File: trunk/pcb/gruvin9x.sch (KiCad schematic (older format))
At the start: 162 parts, among them K1 CONN_3, K2 CONN_3, P1 CONN_5X2, P10 CONN_1, P11 CONN_1, P12 CONN_1, P13 CONN_8, P14 CONN_2, P15 CONN_1, P16 CONN_1, P17 CONN_1, P2 CONN_5, P3 CONN_6, P4 CONN_9, P5 CONN_9, P6 CONN_6, P7 CONN_12, P8 CONN_30, P9 CONN_1, Q1 BC847C, Q2 BC847C, Q3 BC857C, SW1 SW_PUSH, SW2 SW_PUSH, SW3 SW_PUSH, SW4 SW_PUSH, SW5 SW_PUSH, SW6 SW_PUSH, U1 78L05, U2 4066, U3 LN-6206-30, X1 16MHz 18pf

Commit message: Issue 17 fixed
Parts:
- gave numbers to parts that had none: 4
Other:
- note added: "Trim Switches"
- note removed: "Trim Switches (existing wires)"

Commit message: PCB V3 re-routed to corrected V3 schematic (trims + PPM-in inverting buffer). Corrections made to LCD decoupling capacitor values (1uF) on other schematics.
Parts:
- removed C53, C54, C55, C56: 0.1, symbol C
- removed Q4: BC549, SOT23EBD, symbol NPN
- added Q4: BC847C, SOT23-BCE, symbol BC847C
- C46, C47, C48, C49, C50: value 0.1 -> 1u
- R79: value 330 -> 200
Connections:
- wire segments 519 -> 510

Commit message: Code, Schematic and PCB updated to new Timer0 WGM speaker tone output on PB7. (Backlight control moved to PC0. Old timer0 stuff moved to timer2)
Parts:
- removed P15: CONN_1, symbol CONN_1
- added P18: CONN_2, CONN_2MM_2x1, symbol CONN_2
- added R82: 1K0, symbol R
- added R83, R84: 200, symbol R
- P14: footprint (none) -> CONN_2MM_2x1
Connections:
- net labels added: Buzzer, Volume
- net labels removed: Spare2
- wire segments 510 -> 511
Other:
- moved on the sheet: P10

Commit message: Schematic v3.2 updated to include LCD back-light driver mounting posts. PCB v3.2 routed to match.
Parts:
- removed P12: CONN_1, symbol CONN_1
- added K3: CONN_3, symbol CONN_3
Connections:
- wire segments 511 -> 517

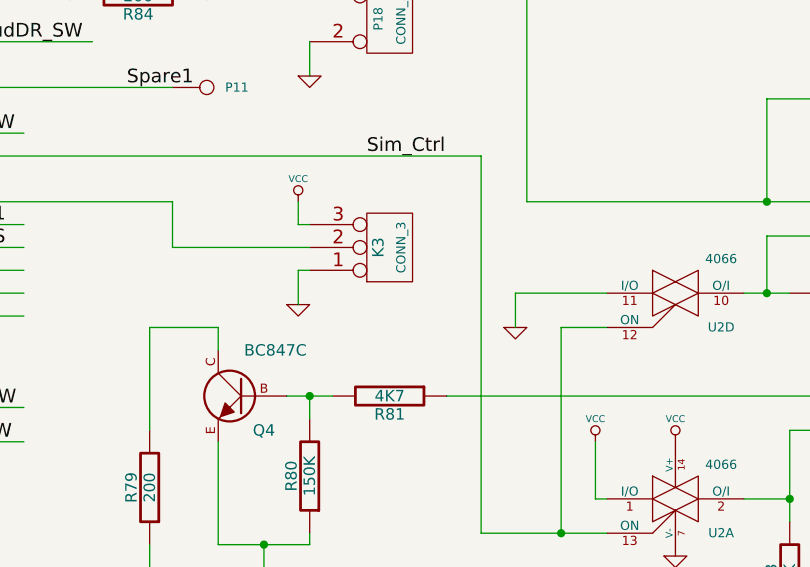
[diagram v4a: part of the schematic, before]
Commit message: Minor V3 schematic edit
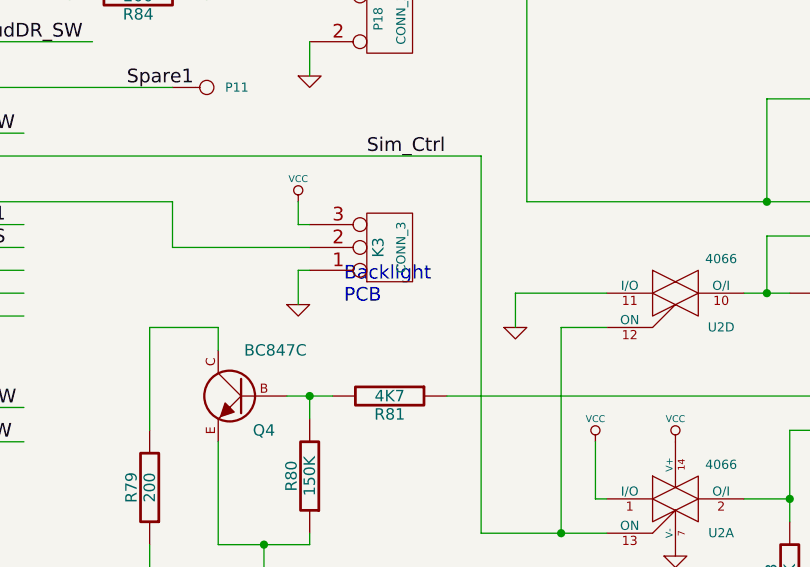
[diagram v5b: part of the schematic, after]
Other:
- note added: "Backlight\nPCB"
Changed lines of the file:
@@
-EESchema Schematic File Version 2  date 16/01/2011 8:05:06 p.m.
+EESchema Schematic File Version 2  date 16/01/2011 9:16:43 p.m.
 LIBS:conn_5
 LIBS:atmega64
@@
 Comment4 "Licensed under the TAPR Open Hardware License (see file,  LICENSE)"
 $EndDescr
+Text Notes 9100 9450 0    60   ~ 0
+Backlight\nPCB
 Wire Wire Line
 	8900 9000 8900 9100

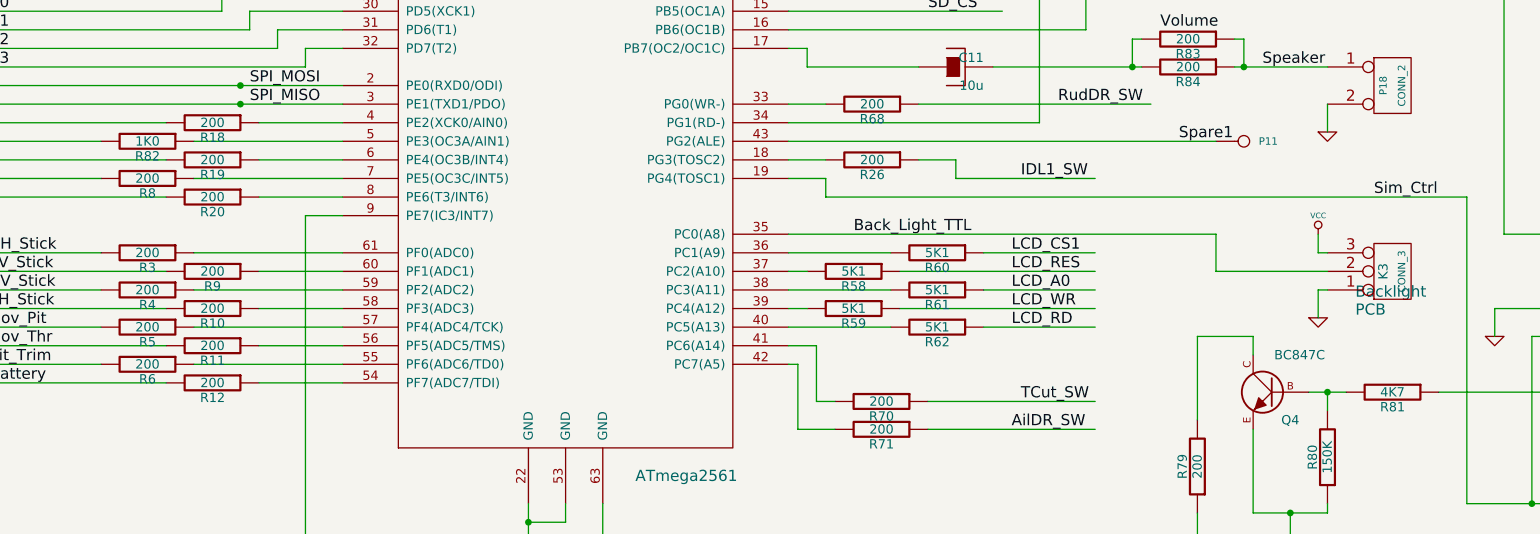
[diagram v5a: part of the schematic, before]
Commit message: PCB edits. BOM updated for new V3 component counts
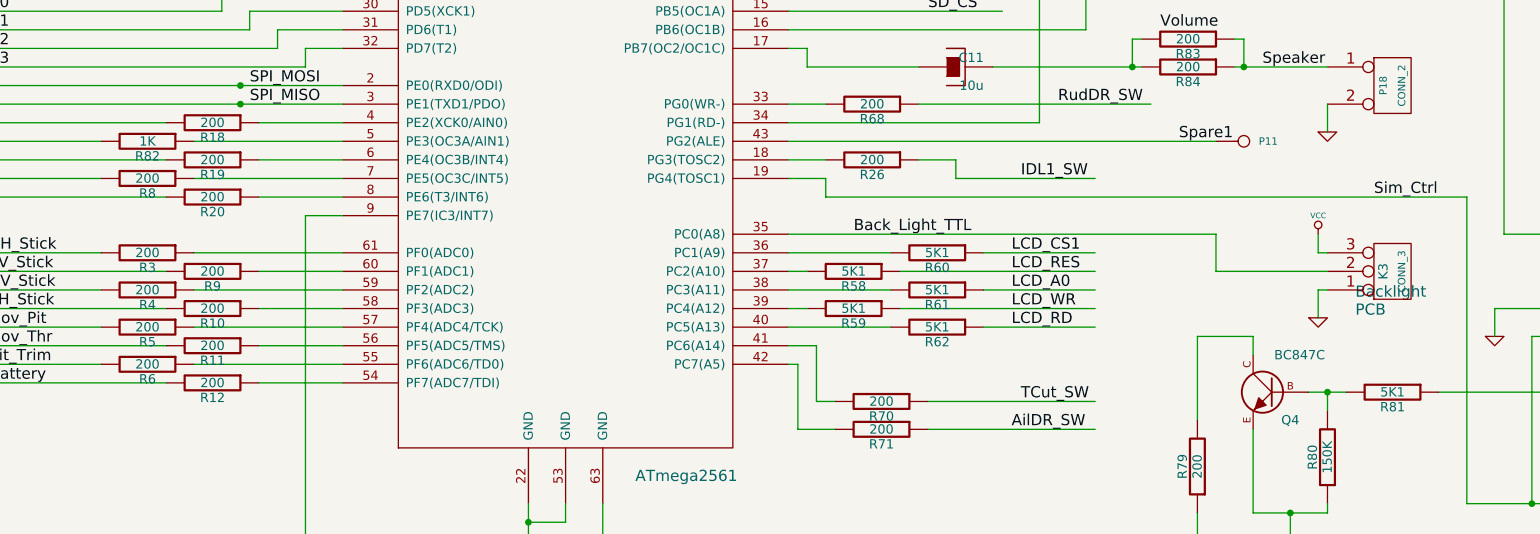
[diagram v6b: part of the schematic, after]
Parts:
- R81: value 4K7 -> 5K1
- R82: value 1K0 -> 1K
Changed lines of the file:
@@
-EESchema Schematic File Version 2  date 16/01/2011 9:16:43 p.m.
+EESchema Schematic File Version 2  date 17/01/2011 3:42:48 p.m.
 LIBS:conn_5
 LIBS:atmega64
@@
 Sheet 1 1
 Title "Main Controller PCB (Stock)"
-Date "16 jan 2011"
+Date "17 jan 2011"
 Rev "3.2"
 Comp ""
@@
 P 2600 8500
 F 0 "R82" V 2680 8500 50  0000 C CNN
-F 1 "1K0" V 2600 8500 50  0000 C CNN
+F 1 "1K" V 2600 8500 50  0000 C CNN
 	1    2600 8500
 	0    1    1    0
@@
 P 9300 9850
 F 0 "R81" V 9380 9850 50  0000 C CNN
-F 1 "4K7" V 9300 9850 50  0000 C CNN
+F 1 "5K1" V 9300 9850 50  0000 C CNN
 	1    9300 9850
 	0    1    1    0

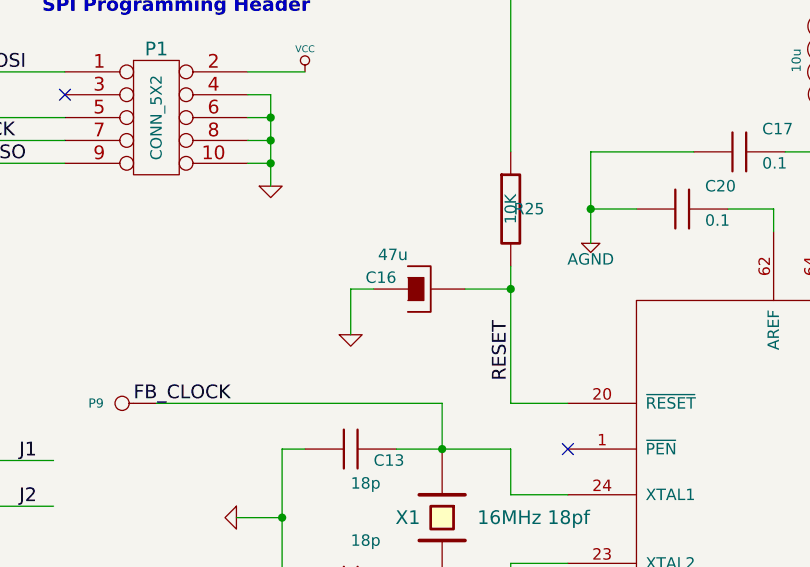
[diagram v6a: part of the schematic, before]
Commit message: Genuine Atmel in-circuit programmers dont like a reset capacitor greater than 10µF. Accordingly, Ive changed the 47µF reset capacitor to 10µF, which still worked reliably under multiple power cycle tests. (And the Atmel AVRISPmkII now works too.)
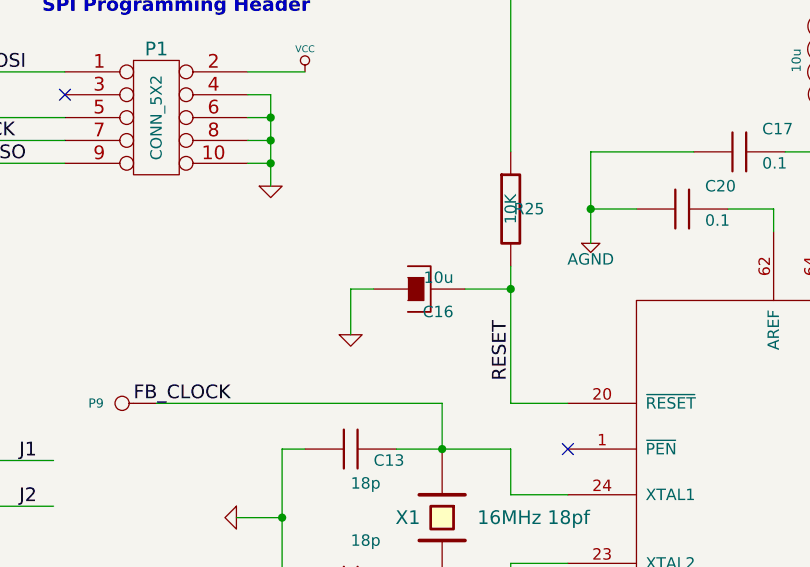
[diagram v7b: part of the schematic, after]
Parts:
- C16: value 47u -> 10u
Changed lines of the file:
@@
-EESchema Schematic File Version 2  date 17/01/2011 3:42:48 p.m.
+EESchema Schematic File Version 2  date 19/01/2011 10:47:29 a.m.
 LIBS:conn_5
 LIBS:atmega64
@@
 Sheet 1 1
 Title "Main Controller PCB (Stock)"
-Date "17 jan 2011"
+Date "18 jan 2011"
 Rev "3.2"
 Comp ""
@@
 U 1 1 4CE74935
 P 3000 5800
-F 0 "C16" V 3050 5900 50  0000 L CNN
-F 1 "47u" V 3150 5850 50  0000 L CNN
+F 0 "C16" V 2900 5650 50  0000 L CNN
+F 1 "10u" V 3050 5650 50  0000 L CNN
 	1    3000 5800
 	0    -1   -1   0

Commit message: PCB V3.3 updated. Includes changes to SD card connector and interface board, which now includes the I2C Real Time Clock chip.
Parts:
- removed P10: CONN_1, symbol CONN_1
- C16: value 10u -> 1u
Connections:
- net labels added: I2C_SCL, I2C_SDA
- net labels removed: SD_Pwr, Spare0
- wire segments 517 -> 514
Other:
- note added: "MM/SD \nCARD (5V!)"
- note removed: "MMC/SDCARD (5V!)"
